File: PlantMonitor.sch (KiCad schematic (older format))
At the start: 2 parts

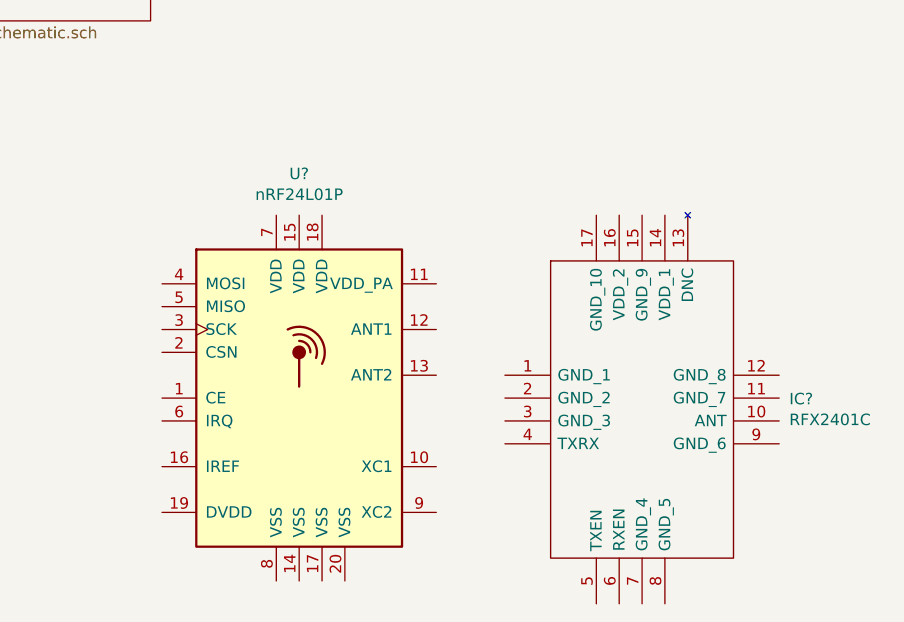
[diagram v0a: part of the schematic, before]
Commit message: First revision of RF circuit
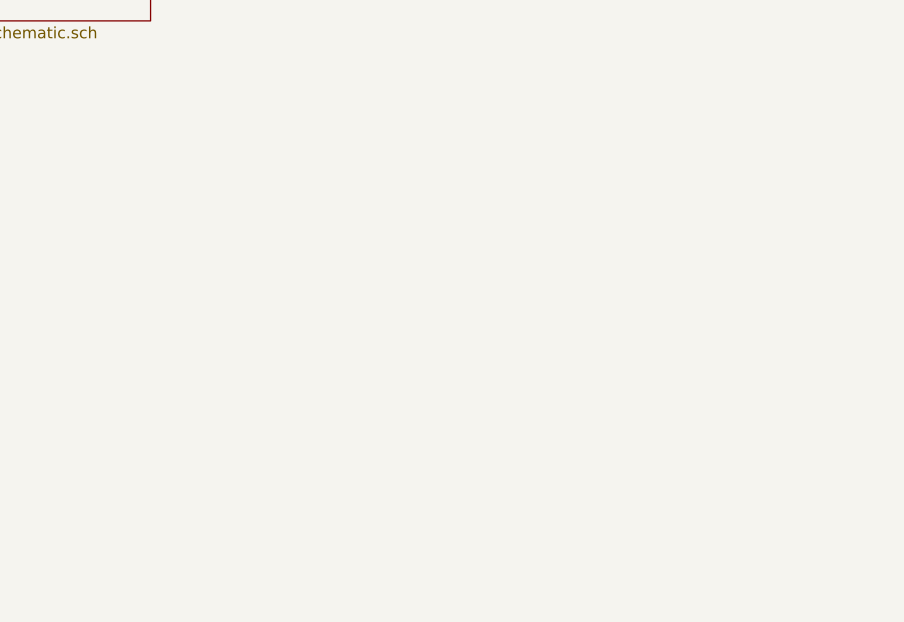
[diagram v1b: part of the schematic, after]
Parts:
- removed IC?: RFX2401C, RFX2401C:QFN50P300X300X60-17N-D, symbol RFX2401C:RFX2401C
- removed U?: nRF24L01P, Package_DFN_QFN:QFN-20-1EP_4x4mm_P0.5mm_EP2.5x2.5mm, symbol RF:nRF24L01P
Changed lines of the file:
@@
 $Descr A4 11693 8268
 encoding utf-8
-Sheet 1 4
+Sheet 1 5
 Title "Plant Monitor"
 Date "2020-06-01"
@@
 Comment4 ""
 $EndDescr
-$Comp
-L RF:nRF24L01P U?
-U 1 1 5ED58AD0
-P 5350 4650
-F 0 "U?" H 5350 5631 50  0000 C CNN
-F 1 "nRF24L01P" H 5350 5540 50  0000 C CNN
-F 2 "Package_DFN_QFN:QFN-20-1EP_4x4mm_P0.5mm_EP2.5x2.5mm" H 5550 5450 50  0001 L CIN
-F 3 "http://www.nordicsemi.com/eng/content/download/2726/34069/file/nRF24L01P_Product_Specification_1_0.pdf" H 5350 4750 50  0001 C CNN
-	1    5350 4650
-	1    0    0    -1
-$EndComp
-$Comp
-L RFX2401C:RFX2401C IC?
-U 1 1 5ED58ADE
-P 6250 4550
-F 0 "IC?" H 7494 4446 50  0000 L CNN
-F 1 "RFX2401C" H 7494 4355 50  0000 L CNN
-F 2 "RFX2401C:QFN50P300X300X60-17N-D" H 7300 5050 50  0001 L CNN
-F 3 "http://www.skyworksinc.com/uploads/documents/RFX2401C_204359A.pdf" H 7300 4950 50  0001 L CNN
-F 4 "RF Front End 2.4GHz ZigBee/ISM RFeIC PA+LNA+SPDT" H 7300 4850 50  0001 L CNN "Description"
-F 5 "0.6" H 7300 4750 50  0001 L CNN "Height"
-F 6 "Skyworks" H 7300 4650 50  0001 L CNN "Manufacturer_Name"
-F 7 "RFX2401C" H 7300 4550 50  0001 L CNN "Manufacturer_Part_Number"
-F 8 "RFX2401C" H 7300 4450 50  0001 L CNN "Arrow Part Number"
-F 9 "" H 7300 4350 50  0001 L CNN "Arrow Price/Stock"
-F 10 "477-RFX2401C" H 7300 4250 50  0001 L CNN "Mouser Part Number"
-F 11 "https://www.mouser.co.uk/ProductDetail/Skyworks-Solutions-Inc/RFX2401C?qs=dBWc1juS%252B3ydEXrKsuxQ7A%3D%3D" H 7300 4150 50  0001 L CNN "Mouser Price/Stock"
-	1    6250 4550
-	1    0    0    -1
-$EndComp
 $Sheet
 S 3500 1500 1000 500
